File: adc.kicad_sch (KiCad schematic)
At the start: 1 part, among them U7 MCP3008

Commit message: finish schematic capture
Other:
- note removed: "Add decoupling caps"
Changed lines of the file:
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@@
 		(comment 4 "Tobe Cynar")
-	)
-	(text "Add decoupling caps\n"
-		(exclude_from_sim no)
-		(at 127 96.52 0)
-		(effects
-			(font
-				(size 1.27 1.27)
-			)
-		)
 	)
 	(text "Add layout features to isolate problems\n"
 		(exclude_from_sim no)
-		(at 142.24 101.6 0)
+		(at 147.32 95.25 0)
 		(effects
 			(font

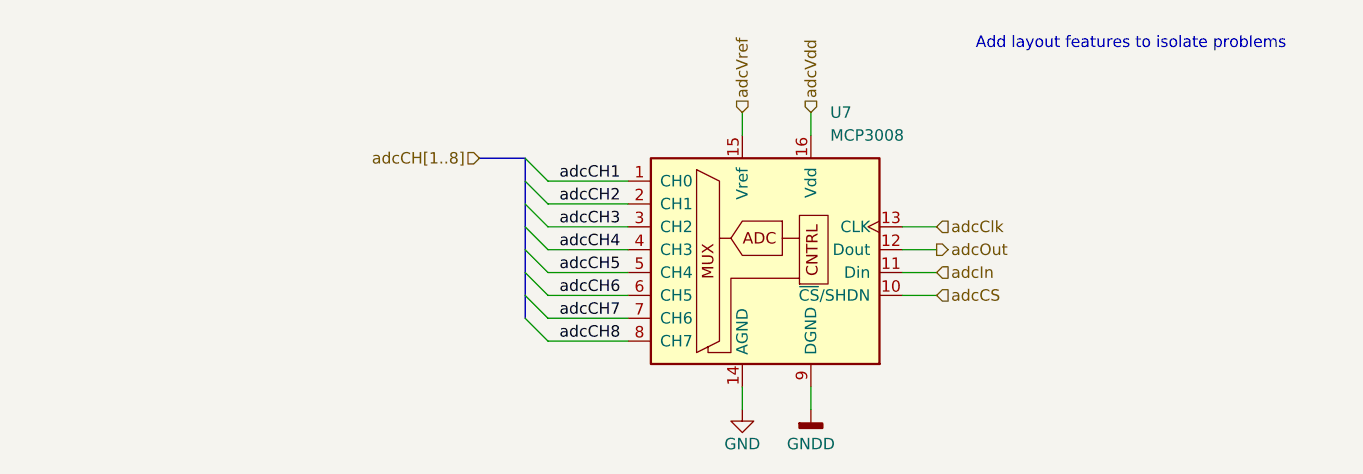
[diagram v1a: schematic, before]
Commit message: add test points throughout the schematic
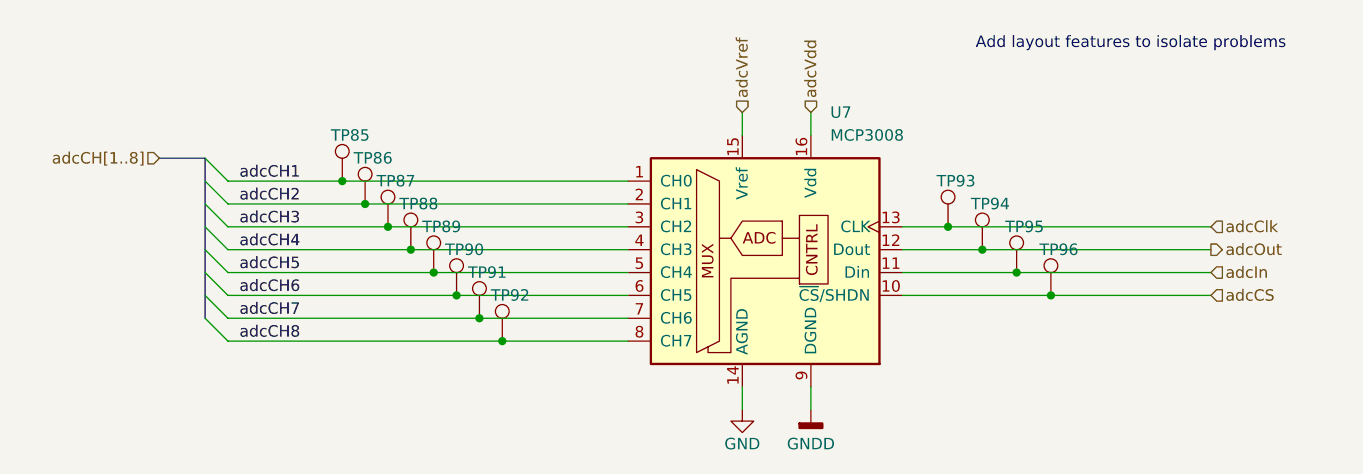
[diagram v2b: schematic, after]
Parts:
- added TP85, TP86, TP87, TP88, TP89, TP90, TP91, TP92, TP93, TP94, TP95, TP96: TestPoint, Testpoints:M5_3in1_TestPoint, symbol Connector:TestPoint
- U7: footprint (none) -> Package_DIP:DIP-16_W7.62mm
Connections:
- net adcCH1: now also TP85.1
- net adcCH2: now also TP86.1
- net adcCH3: now also TP87.1
- net adcCH4: now also TP88.1
- net adcCH5: now also TP89.1
- net adcCH6: now also TP90.1
- net adcCH7: now also TP91.1
- net adcCH8: now also TP92.1
- net adcCS: now also TP96.1
- net adcClk: now also TP93.1
- net adcIn: now also TP95.1
- net adcOut: now also TP94.1

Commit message: finish initial schematic design, start pcb layout
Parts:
- U7: DKPN (none) -> MCP3008-I/P-ND
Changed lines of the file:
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@@
 		(in_pos_files yes)
 		(dnp no)
-		(property "Reference" "#PWR?"
+		(property "Reference" "#PWR0112"
 			(at 104.14 142.24 0)
 			(hide yes)
@@
 			(project "pbx-sniffer-v2"
 				(path "/eb421281-26a1-483f-b39a-0425ec8eb8df/ff2bf5b0-8d55-4ab2-beca-8dca5e42da3e"
-					(reference "#PWR?")
+					(reference "#PWR0112")
 					(unit 1)
 				)
@@
 			)
 		)
+		(property "DKPN" "MCP3008-I/P-ND"
+			(at 106.68 118.11 0)
+			(hide yes)
+			(show_name no)
+			(do_not_autoplace no)
+			(effects
+				(font
+					(size 1.27 1.27)
+				)
+			)
+		)
 		(pin "2"
 		)
@@
 		(dnp no)
 		(fields_autoplaced yes)
-		(property "Reference" "#PWR?"
+		(property "Reference" "#PWR0113"
 			(at 111.76 142.24 0)
 			(hide yes)
@@
 			(project "pbx-sniffer-v2"
 				(path "/eb421281-26a1-483f-b39a-0425ec8eb8df/ff2bf5b0-8d55-4ab2-beca-8dca5e42da3e"
-					(reference "#PWR?")
-					(unit 1)
-				)
+					(reference "#PWR0113")
+					(unit 1)
+				)

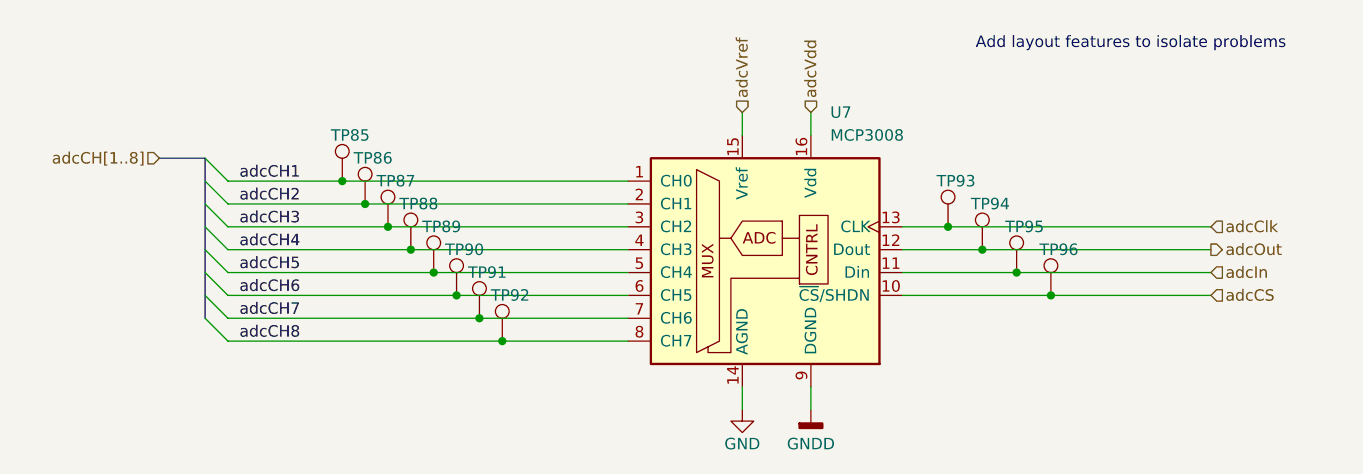
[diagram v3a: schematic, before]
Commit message: place footprints for one line module
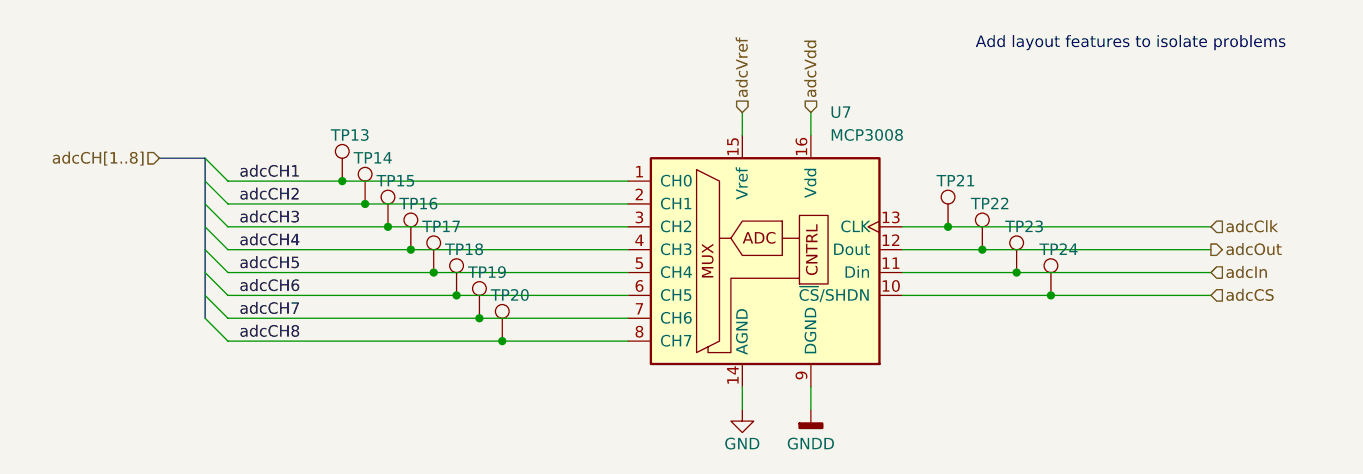
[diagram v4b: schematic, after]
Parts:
- renumbered TP85 to TP13, TP86 to TP14, TP87 to TP15, TP88 to TP16, TP89 to TP17, TP90 to TP18, TP91 to TP19, TP92 to TP20, TP93 to TP21, TP94 to TP22, TP95 to TP23, TP96 to TP24
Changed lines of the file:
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@@
 		(in_pos_files yes)
 		(dnp no)
-		(property "Reference" "TP94"
+		(property "Reference" "TP22"
 			(at 129.54 113.03 0)
 			(show_name no)
@@
 			(project "pbx-sniffer-v2"
 				(path "/eb421281-26a1-483f-b39a-0425ec8eb8df/ff2bf5b0-8d55-4ab2-beca-8dca5e42da3e"
-					(reference "TP94")
+					(reference "TP22")
 					(unit 1)
 				)
@@
 		(in_pos_files yes)
 		(dnp no)
-		(property "Reference" "TP85"
+		(property "Reference" "TP13"
 			(at 58.42 105.41 0)
 			(show_name no)
@@
 			(project "pbx-sniffer-v2"
 				(path "/eb421281-26a1-483f-b39a-0425ec8eb8df/ff2bf5b0-8d55-4ab2-beca-8dca5e42da3e"
-					(reference "TP85")
+					(reference "TP13")
 					(unit 1)
 				)
@@
 		(in_pos_files yes)
 		(dnp no)
-		(property "Reference" "TP91"
+		(property "Reference" "TP19"
 			(at 73.66 120.65 0)
 			(show_name no)
@@
 			(project "pbx-sniffer-v2"
 				(path "/eb421281-26a1-483f-b39a-0425ec8eb8df/ff2bf5b0-8d55-4ab2-beca-8dca5e42da3e"
-					(reference "TP91")
+					(reference "TP19")
 					(unit 1)
 				)
@@
 		(in_pos_files yes)
 		(dnp no)
-		(property "Reference" "TP86"
+		(property "Reference" "TP14"
 			(at 60.96 107.95 0)
 			(show_name no)
@@
 			(project "pbx-sniffer-v2"
 				(path "/eb421281-26a1-483f-b39a-0425ec8eb8df/ff2bf5b0-8d55-4ab2-beca-8dca5e42da3e"
-					(reference "TP86")
+					(reference "TP14")
 					(unit 1)
 				)
@@
 		(in_pos_files yes)
 		(dnp no)
-		(property "Reference" "#PWR0112"
+		(property "Reference" "#PWR032"
 			(at 104.14 142.24 0)
 			(hide yes)
@@
 			(project "pbx-sniffer-v2"
 				(path "/eb421281-26a1-483f-b39a-0425ec8eb8df/ff2bf5b0-8d55-4ab2-beca-8dca5e42da3e"
-					(reference "#PWR0112")
+					(reference "#PWR032")
 					(unit 1)
 				)
@@
 		(in_pos_files yes)
 		(dnp no)
-		(property "Reference" "TP89"
+		(property "Reference" "TP17"
 			(at 68.58 115.57 0)
 			(show_name no)
@@
 			(project "pbx-sniffer-v2"
 				(path "/eb421281-26a1-483f-b39a-0425ec8eb8df/ff2bf5b0-8d55-4ab2-beca-8dca5e42da3e"
-					(reference "TP89")
+					(reference "TP17")
 					(unit 1)
 				)
@@
 		(in_pos_files yes)
 		(dnp no)
-		(property "Reference" "TP87"
+		(property "Reference" "TP15"
 			(at 63.5 110.49 0)
 			(show_name no)
@@
 			(project "pbx-sniffer-v2"
 				(path "/eb421281-26a1-483f-b39a-0425ec8eb8df/ff2bf5b0-8d55-4ab2-beca-8dca5e42da3e"
-					(reference "TP87")
+					(reference "TP15")
 					(unit 1)
 				)
@@
 		(in_pos_files yes)
 		(dnp no)
-		(property "Reference" "TP90"
+		(property "Reference" "TP18"
 			(at 71.12 118.11 0)
 			(show_name no)
@@
 			(project "pbx-sniffer-v2"
 				(path "/eb421281-26a1-483f-b39a-0425ec8eb8df/ff2bf5b0-8d55-4ab2-beca-8dca5e42da3e"
-					(reference "TP90")
+					(reference "TP18")
 					(unit 1)
 				)
@@
 		(in_pos_files yes)
 		(dnp no)
-		(property "Reference" "TP96"
+		(property "Reference" "TP24"
 			(at 137.16 118.11 0)
 			(show_name no)
@@
 			(project "pbx-sniffer-v2"
 				(path "/eb421281-26a1-483f-b39a-0425ec8eb8df/ff2bf5b0-8d55-4ab2-beca-8dca5e42da3e"
-					(reference "TP96")
+					(reference "TP24")
 					(unit 1)
 				)
@@
 		(in_pos_files yes)
 		(dnp no)
-		(property "Reference" "TP95"
+		(property "Reference" "TP23"
 			(at 133.35 115.57 0)
 			(show_name no)
@@
 			(project "pbx-sniffer-v2"
 				(path "/eb421281-26a1-483f-b39a-0425ec8eb8df/ff2bf5b0-8d55-4ab2-beca-8dca5e42da3e"
-					(reference "TP95")
+					(reference "TP23")
 					(unit 1)
 				)
@@
 		(dnp no)
 		(fields_autoplaced yes)
-		(property "Reference" "#PWR0113"
+		(property "Reference" "#PWR033"
 			(at 111.76 142.24 0)
 			(hide yes)
@@
 			(project "pbx-sniffer-v2"
 				(path "/eb421281-26a1-483f-b39a-0425ec8eb8df/ff2bf5b0-8d55-4ab2-beca-8dca5e42da3e"
-					(reference "#PWR0113")
+					(reference "#PWR033")
 					(unit 1)
 				)
@@
 		(in_pos_files yes)
 		(dnp no)
-		(property "Reference" "TP92"
+		(property "Reference" "TP20"
 			(at 76.2 123.19 0)
 			(show_name no)
@@
 			(project "pbx-sniffer-v2"
 				(path "/eb421281-26a1-483f-b39a-0425ec8eb8df/ff2bf5b0-8d55-4ab2-beca-8dca5e42da3e"
-					(reference "TP92")
+					(reference "TP20")
 					(unit 1)
 				)
@@
 		(in_pos_files yes)
 		(dnp no)
-		(property "Reference" "TP88"
+		(property "Reference" "TP16"
 			(at 66.04 113.03 0)
 			(show_name no)
@@
 			(project "pbx-sniffer-v2"
 				(path "/eb421281-26a1-483f-b39a-0425ec8eb8df/ff2bf5b0-8d55-4ab2-beca-8dca5e42da3e"
-					(reference "TP88")
+					(reference "TP16")
 					(unit 1)
 				)
@@
 		(in_pos_files yes)
 		(dnp no)
-		(property "Reference" "TP93"
+		(property "Reference" "TP21"
 			(at 125.73 110.49 0)
 			(show_name no)
@@
 			(project "pbx-sniffer-v2"
 				(path "/eb421281-26a1-483f-b39a-0425ec8eb8df/ff2bf5b0-8d55-4ab2-beca-8dca5e42da3e"
-					(reference "TP93")
-					(unit 1)
-				)
+					(reference "TP21")
+					(unit 1)
+				)
